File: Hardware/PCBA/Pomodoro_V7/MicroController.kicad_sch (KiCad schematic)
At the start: 1 part, among them IC1 ESP32-S2-MINI-2-N4

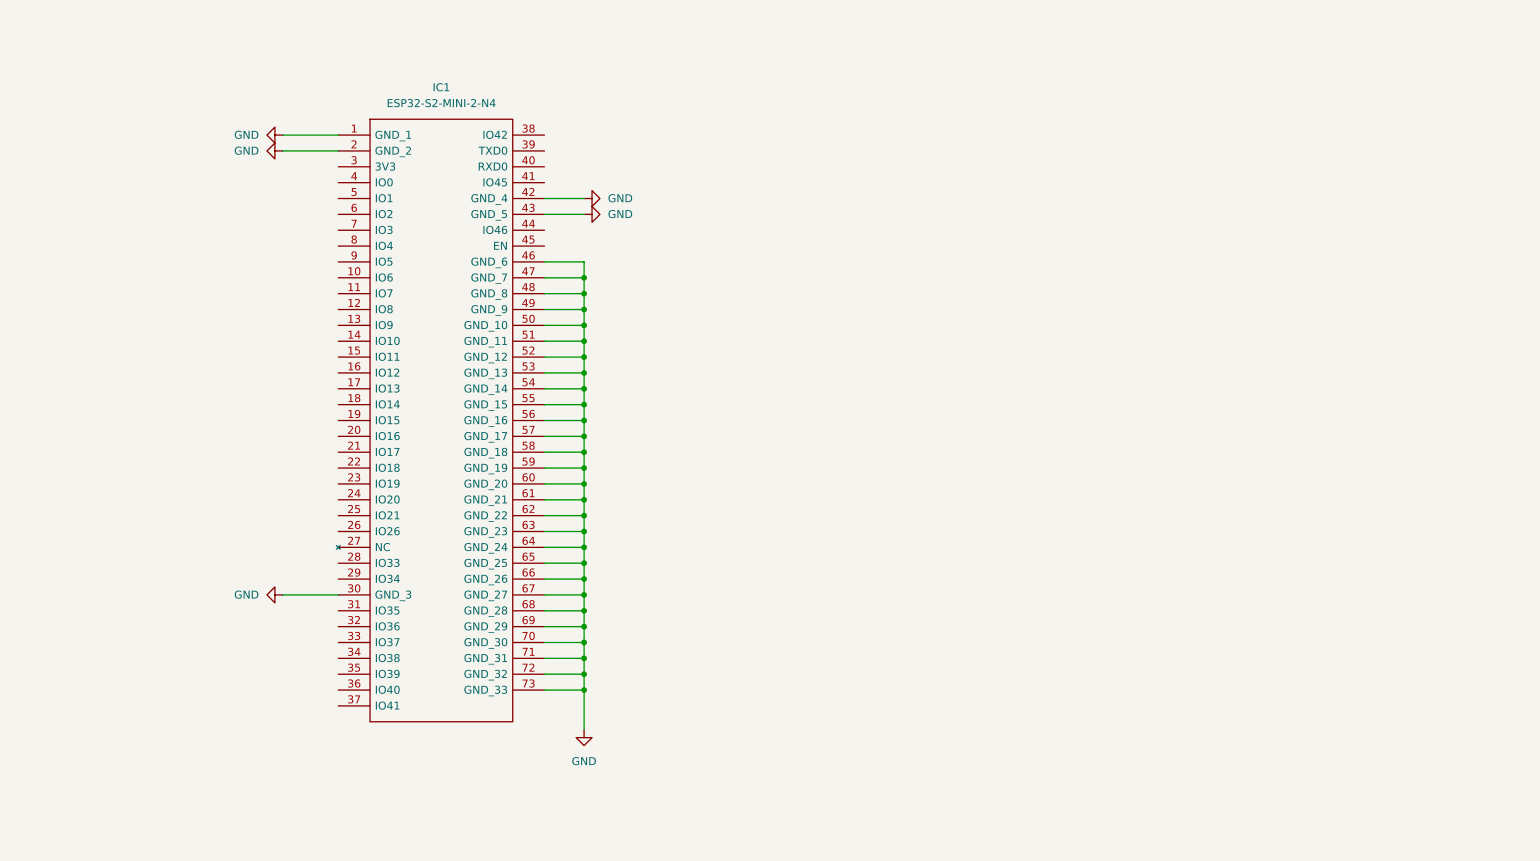
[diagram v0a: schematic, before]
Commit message: Verified the microcontroller Pinout; Added basic peripheral wiring; Added the USBC Wiring
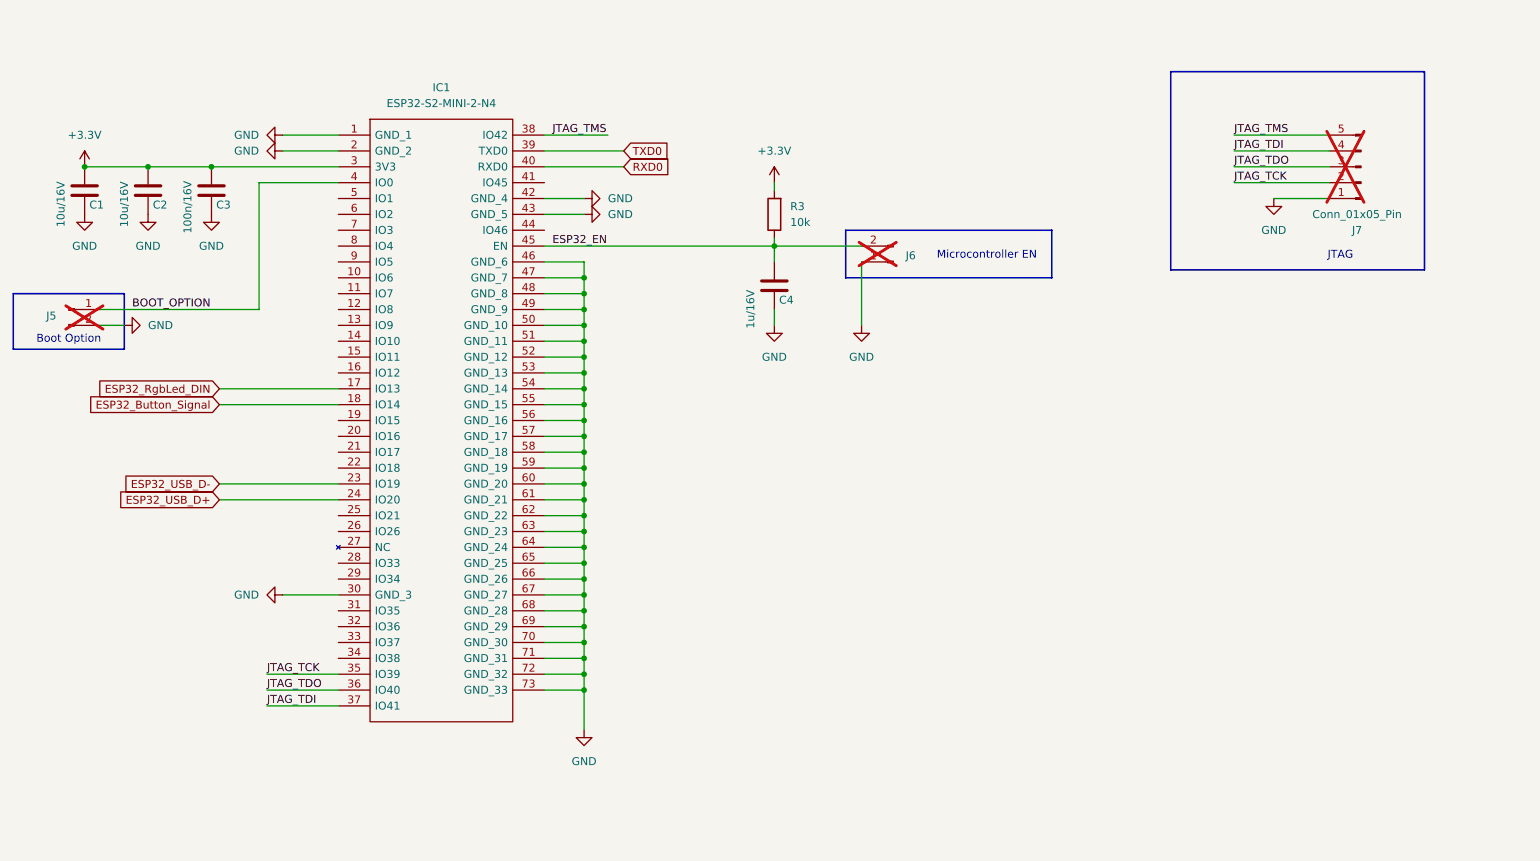
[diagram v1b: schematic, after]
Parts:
- added C1, C2: 10u/16V, Capacitor_SMD:C_0805_2012Metric, symbol Device:C
- added C3: 100n/16V, Capacitor_SMD:C_0805_2012Metric, symbol Device:C
- added C4: 1u/16V, Capacitor_SMD:C_0805_2012Metric, symbol Device:C
- added J5, J6: Conn_01x02_Pin, symbol Connector:Conn_01x02_Pin
- added J7: Conn_01x05_Pin, symbol Connector:Conn_01x05_Pin
- added R3: 10k, Resistor_SMD:R_0805_2012Metric, symbol Device:R
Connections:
- net GND: now also C1.2, C2.2, C3.2, C4.2, J5.2 (Pin_2), J6.1 (Pin_1), J7.1 (Pin_1)
- net ESP32_RgbLed_DIN: now reaches IC1.17 (IO13)
- net ESP32_Button_Signal: now reaches IC1.18 (IO14)
- net ESP32_USB_D-: now reaches IC1.23 (IO19)
- net ESP32_USB_D+: now reaches IC1.24 (IO20)
- net +3.3V: now reaches IC1.3 (3V3)
- net +3.3V: now also C1.1, C2.1, C3.1, R3.2
- net JTAG_TCK: now reaches IC1.35 (IO39)
- net JTAG_TCK: now also J7.2 (Pin_2)
- net JTAG_TDO: now reaches IC1.36 (IO40)
- net JTAG_TDO: now also J7.3 (Pin_3)
- net JTAG_TDI: now reaches IC1.37 (IO41)
- net JTAG_TDI: now also J7.4 (Pin_4)
- net JTAG_TMS: now reaches IC1.38 (IO42)
- net JTAG_TMS: now also J7.5 (Pin_5)
- net TXD0: now reaches IC1.39 (TXD0)
- net BOOT_OPTION: now reaches IC1.4 (IO0)
- net BOOT_OPTION: now also J5.1 (Pin_1)
- net RXD0: now reaches IC1.40 (RXD0)
- net ESP32_EN: now reaches IC1.45 (EN)
- net ESP32_EN: now also C4.1, J6.2 (Pin_2), R3.1
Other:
- note added: "Boot Option"
- note added: "JTAG"
- note added: "Microcontroller EN"

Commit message: FW can now be flashed to an ESP32-S2 Target; Completed the Schematic
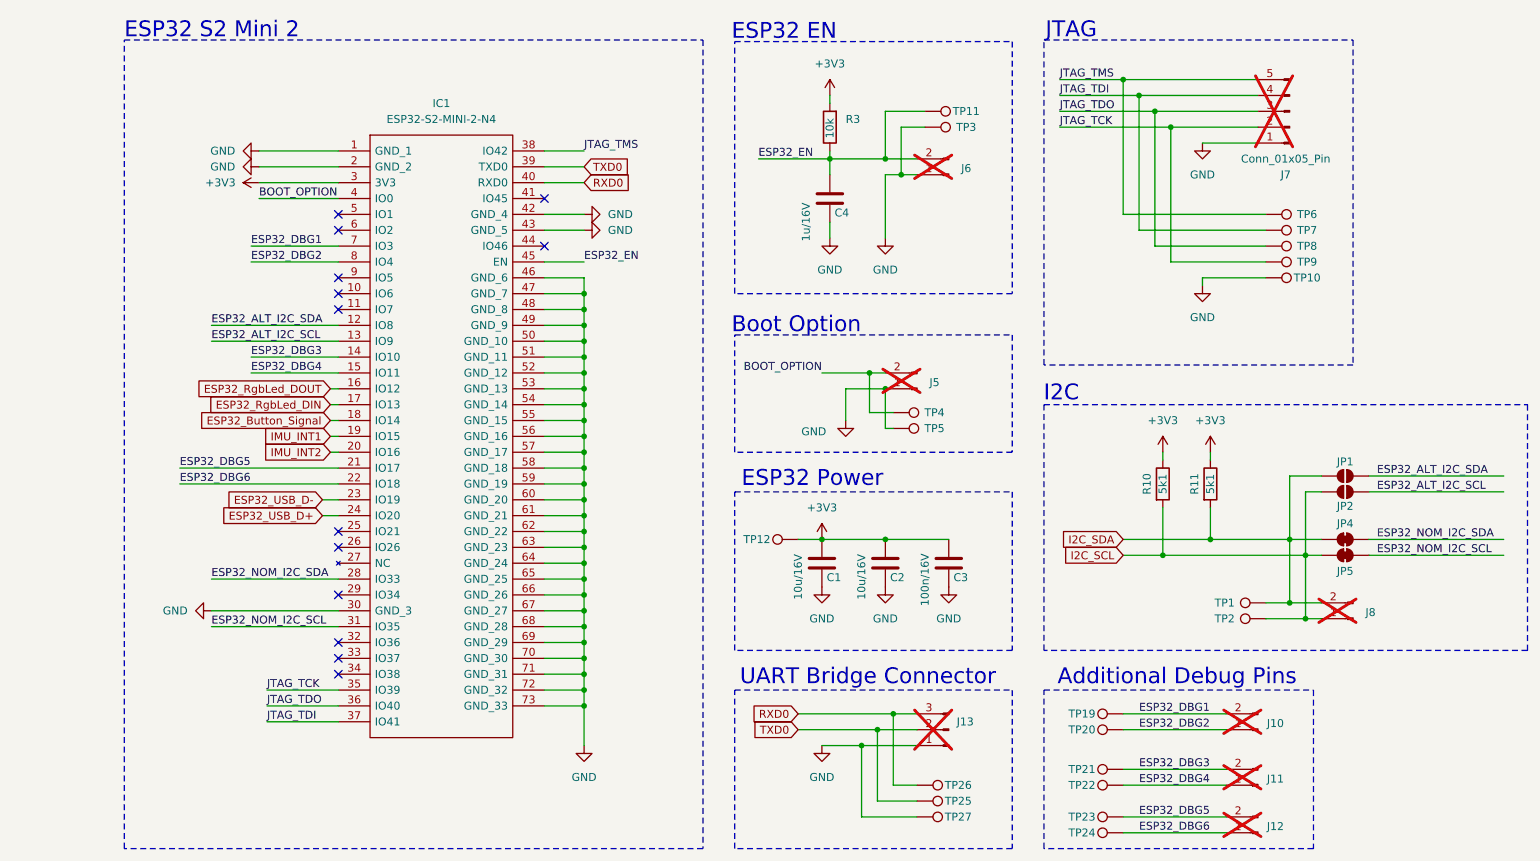
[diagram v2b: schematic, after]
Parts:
- added J10, J11, J12, J8: Conn_01x02_Pin, Connector_PinHeader_2.54mm:PinHeader_1x02_P2.54mm_Vertical, symbol Connector:Conn_01x02_Pin
- added J13: Conn_01x03_Pin, Connector_PinHeader_2.54mm:PinHeader_1x03_P2.54mm_Vertical, symbol Connector:Conn_01x03_Pin
- added JP1, JP2: SolderJumper_2_Open, Jumper:SolderJumper-2_P1.3mm_Open_RoundedPad1.0x1.5mm, symbol Jumper:SolderJumper_2_Open
- added JP4, JP5: SolderJumper_2_Bridged, Jumper:SolderJumper-2_P1.3mm_Bridged2Bar_RoundedPad1.0x1.5mm, symbol Jumper:SolderJumper_2_Bridged
- added R10, R11: 5k1, Resistor_SMD:R_0805_2012Metric, symbol Device:R
- added TP1, TP10, TP11, TP12, TP19, TP2, TP20, TP21, TP22, TP23, TP24, TP25, TP26, TP27, TP3, TP4, TP5, TP6, TP7, TP8, TP9: TestPoint, TestPoint:TestPoint_Pad_D1.0mm, symbol Connector:TestPoint
- IC1: footprint ESP32S2MINI2N4 -> RF_Module:ESP32-S2-MINI-1
- J5, J6: footprint (none) -> Connector_PinHeader_2.54mm:PinHeader_1x02_P2.54mm_Vertical
- J7: footprint (none) -> Connector_PinHeader_2.54mm:PinHeader_1x05_P2.54mm_Vertical
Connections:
- net BOOT_OPTION: now also J5.2 (Pin_2), TP4.1; no longer J5.1 (Pin_1)
- net ESP32_EN: now also TP11.1
- net GND: now also J5.1 (Pin_1), J13.1 (Pin_1), TP10.1, TP27.1, TP3.1, TP5.1; no longer J5.2 (Pin_2)
- net JTAG_TCK: now also TP9.1
- net JTAG_TDI: now also TP7.1
- net JTAG_TDO: now also TP8.1
- net JTAG_TMS: now also TP6.1
- net RXD0: now also J13.3 (Pin_3), TP26.1
- net TXD0: now also J13.2 (Pin_2), TP25.1
- net ESP32_ALT_I2C_SDA: now reaches IC1.12 (IO8)
- net ESP32_ALT_I2C_SDA: now also JP1.2 (B)
- net ESP32_ALT_I2C_SCL: now reaches IC1.13 (IO9)
- net ESP32_ALT_I2C_SCL: now also JP2.1 (A)
- net ESP32_DBG3: now reaches IC1.14 (IO10)
- net ESP32_DBG3: now also J11.2 (Pin_2), TP21.1
- net ESP32_DBG4: now reaches IC1.15 (IO11)
- net ESP32_DBG4: now also J11.1 (Pin_1), TP22.1
- net ESP32_RgbLed_DOUT: now reaches IC1.16 (IO12)
- net IMU_INT1: now reaches IC1.19 (IO15)
- net IMU_INT2: now reaches IC1.20 (IO16)
- net ESP32_DBG5: now reaches IC1.21 (IO17)
- net ESP32_DBG5: now also J12.2 (Pin_2), TP23.1
- net ESP32_DBG6: now reaches IC1.22 (IO18)
- net ESP32_DBG6: now also J12.1 (Pin_1), TP24.1
- net ESP32_NOM_I2C_SDA: now reaches IC1.28 (IO33)
- net ESP32_NOM_I2C_SDA: now also JP4.2 (B)
- net ESP32_NOM_I2C_SCL: now reaches IC1.31 (IO35)
- net ESP32_NOM_I2C_SCL: now also JP5.1 (A)
- net ESP32_DBG1: now reaches IC1.7 (IO3)
- net ESP32_DBG1: now also J10.2 (Pin_2), TP19.1
- net ESP32_DBG2: now reaches IC1.8 (IO4)
- net ESP32_DBG2: now also J10.1 (Pin_1), TP20.1
- net +3.3V renamed +3V3
- net +3V3: now also R10.1, R11.1, TP12.1
- new net I2C_SCL: J8.1 (Pin_1), JP2.2 (B), JP5.2 (B), R10.2, TP2.1
- new net I2C_SDA: J8.2 (Pin_2), JP1.1 (A), JP4.1 (A), R11.2, TP1.1
- no-connect marks 0 -> 13
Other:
- note added: "Additional Debug Pins"
- note added: "ESP32 EN"
- note added: "ESP32 Power"
- note added: "ESP32 S2 Mini 2"
- note added: "I2C"
- note added: "UART Bridge Connector"
- note removed: "Microcontroller EN"
- moved on the sheet: C4, IC1, J5, J7, R3

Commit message: added the selector wheel, changed the Connectors on the Trigger Button to move the assemlby closer together
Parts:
- R10, R11: value 5k1 -> 5k1(1%)
- R3: value 10k -> 10k(1%); MPN (none) -> CR0805-FX-5101ELF; Part ID (none) -> CR0805-FX-5101ELF
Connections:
- net +3V3: now also R10.2, R11.2; no longer R10.1, R11.1
- net I2C_SCL: now also R10.1; no longer R10.2
- net I2C_SDA: now also R11.1; no longer R11.2
- net ESP32_ADC_POTI: now reaches IC1.5 (IO1)
- no-connect marks 13 -> 12

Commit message: Update on the PCBA
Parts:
- removed TP12: TestPoint, TestPoint:TestPoint_Pad_D1.0mm, symbol Connector:TestPoint
- renumbered C4 to C1, C1 to C2, C2 to C3, C3 to C4, J7 to J1, J6 to J2, J5 to J3, J8 to J4, J13 to J5, J10 to J6, J11 to J7, J12 to J8, JP4 to JP3, JP5 to JP4, R3 to R1, R10 to R2, R11 to R3, TP11 to TP1, TP1 to TP11, TP2 to TP12, TP19 to TP13, TP20 to TP14, TP21 to TP15, TP26 to TP16, TP22 to TP17, TP25 to TP18, TP27 to TP19, TP3 to TP2, TP23 to TP20, TP24 to TP21, TP6 to TP3, TP7 to TP4, TP8 to TP5, TP9 to TP6, TP10 to TP7, TP4 to TP8, TP5 to TP9

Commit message: Updated the PCBA Files
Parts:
- C1: value 1u/16V -> 1u/16V+/X5R
- C2, C3: value 10u/16V -> 10u/16V+/X5R
- C4: value 100n/16V -> 100n/16V+/X5R
- IC1: Mfg Part # (none) -> ESP32-S2-MINI-2-N4
- JP1, JP2, JP3, JP4, TP1, TP11, TP12, TP13, TP14, TP15, TP16, TP17, TP18, TP19, TP2, TP20, TP21, TP3, TP4, TP5, TP6, TP7, TP8, TP9: now not fitted
